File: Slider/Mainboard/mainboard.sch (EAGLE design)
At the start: 57 parts, among them IC1 7805TV, IC2 33CV, IC3 LM358, SW1 MS MOT1, SW2 MS MOT2, T1 BC337, T2 BC337, U1 ATMEGA328P_PDIP, U2 MAX232PTH

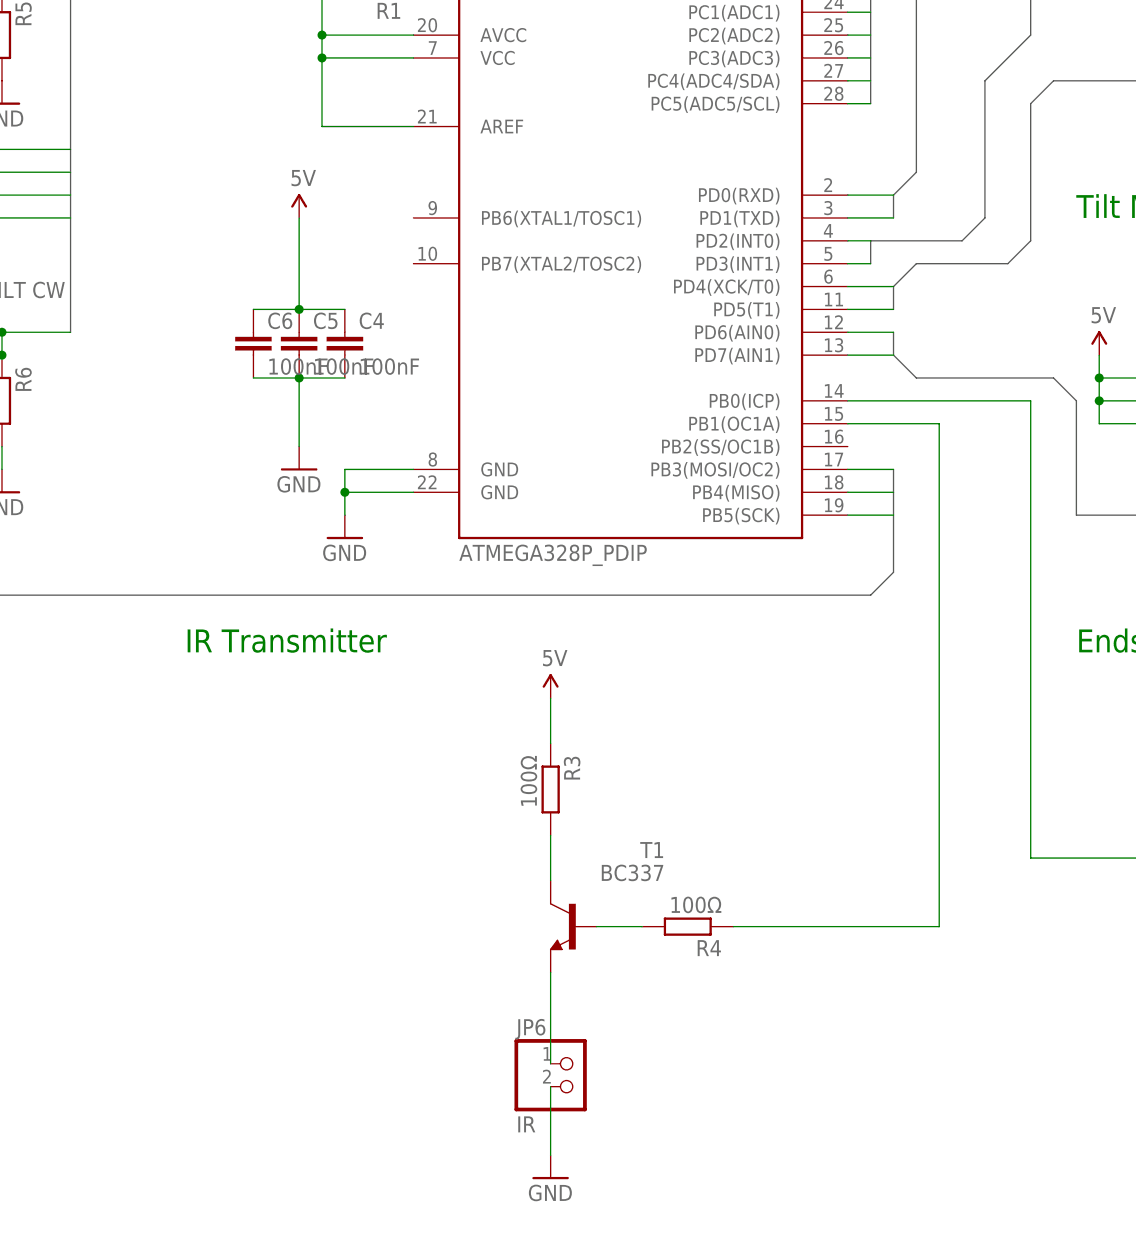
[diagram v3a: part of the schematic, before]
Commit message: added 16 MHZ Crystal with throughhole footprint
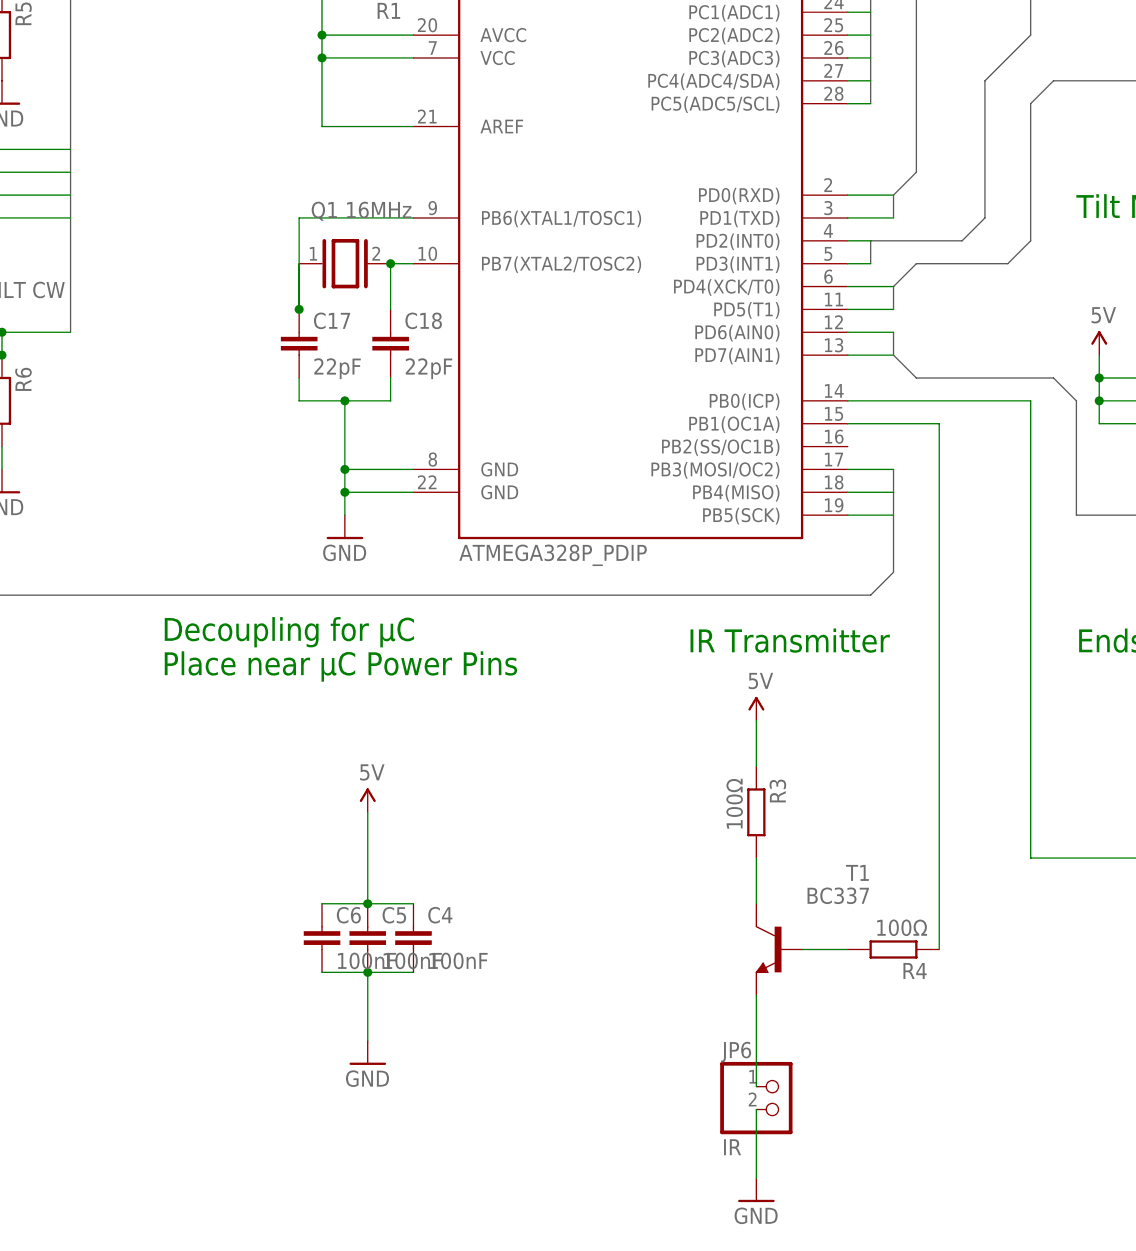
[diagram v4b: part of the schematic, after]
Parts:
- added C17, C18: 22pF, rcl:C-EU050-024X044
- added Q1: 16MHz, special:XTAL/S
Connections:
- new net N$39: C18.1, Q1.2, U1.PB7(XTAL2/TOSC2)
- new net N$40: C17.1, Q1.1, U1.PB6(XTAL1/TOSC1)
- net GND: now also C17.2, C18.2
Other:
- note added: "Decoupling for µC Place near µC Power Pins"
- moved on the sheet: C4, C5, C6, JP6, R3, R4, T1
